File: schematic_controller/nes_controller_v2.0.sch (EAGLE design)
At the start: 22 parts

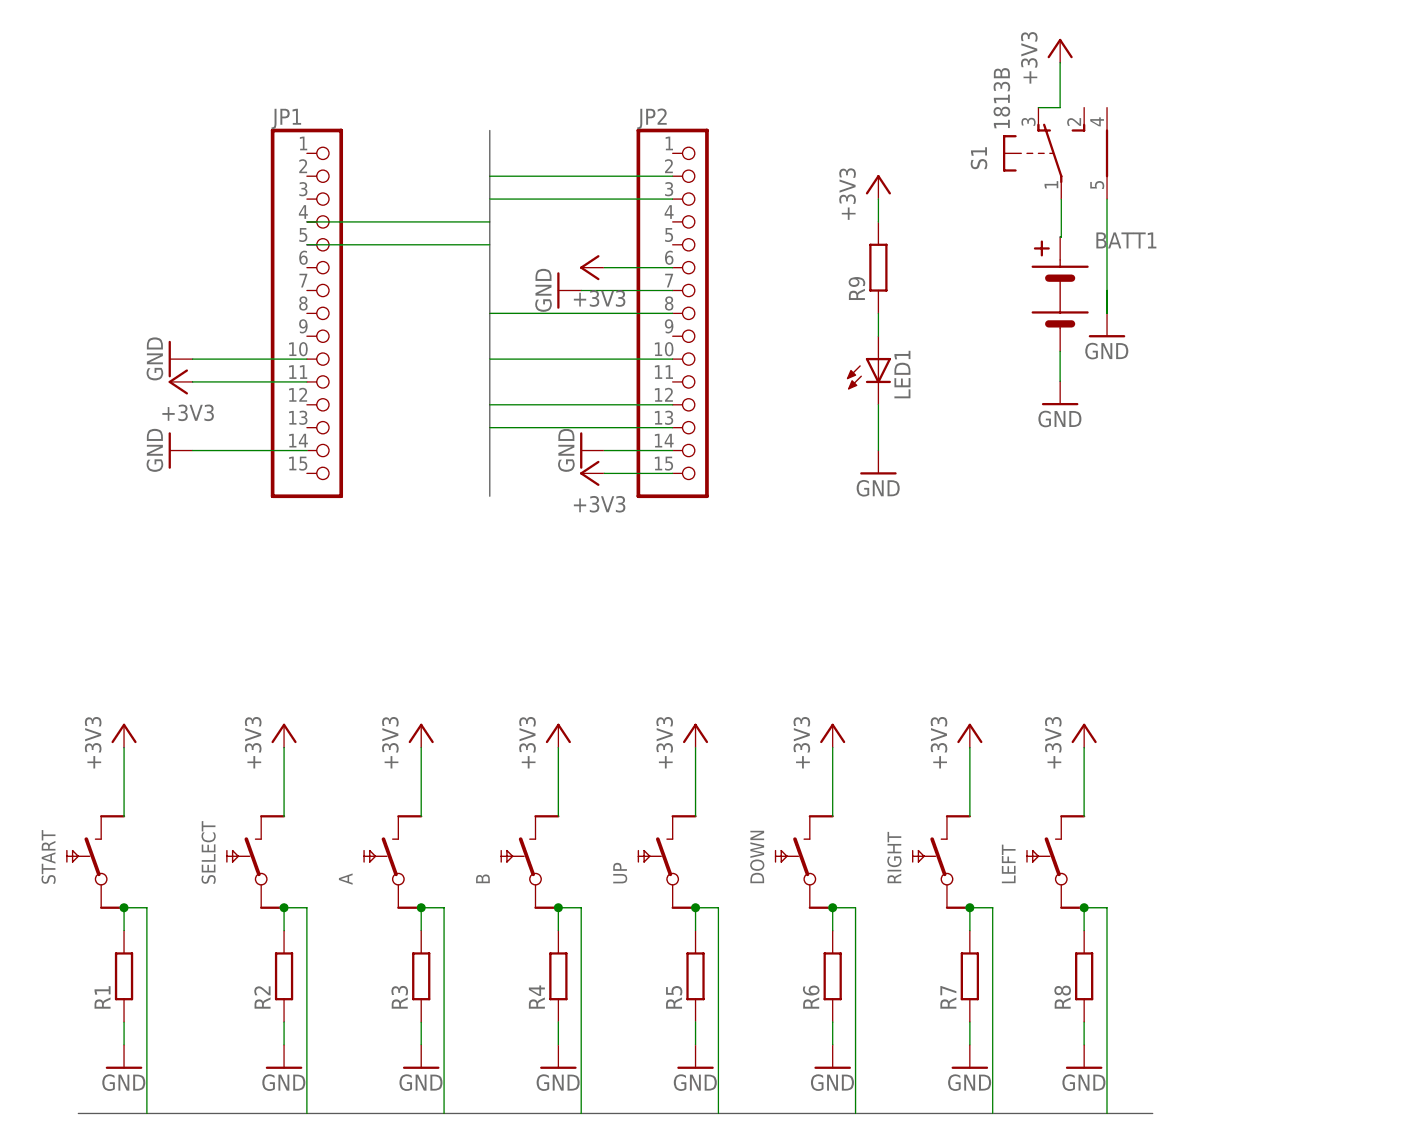
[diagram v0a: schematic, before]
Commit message: changed schematic and boart to v2
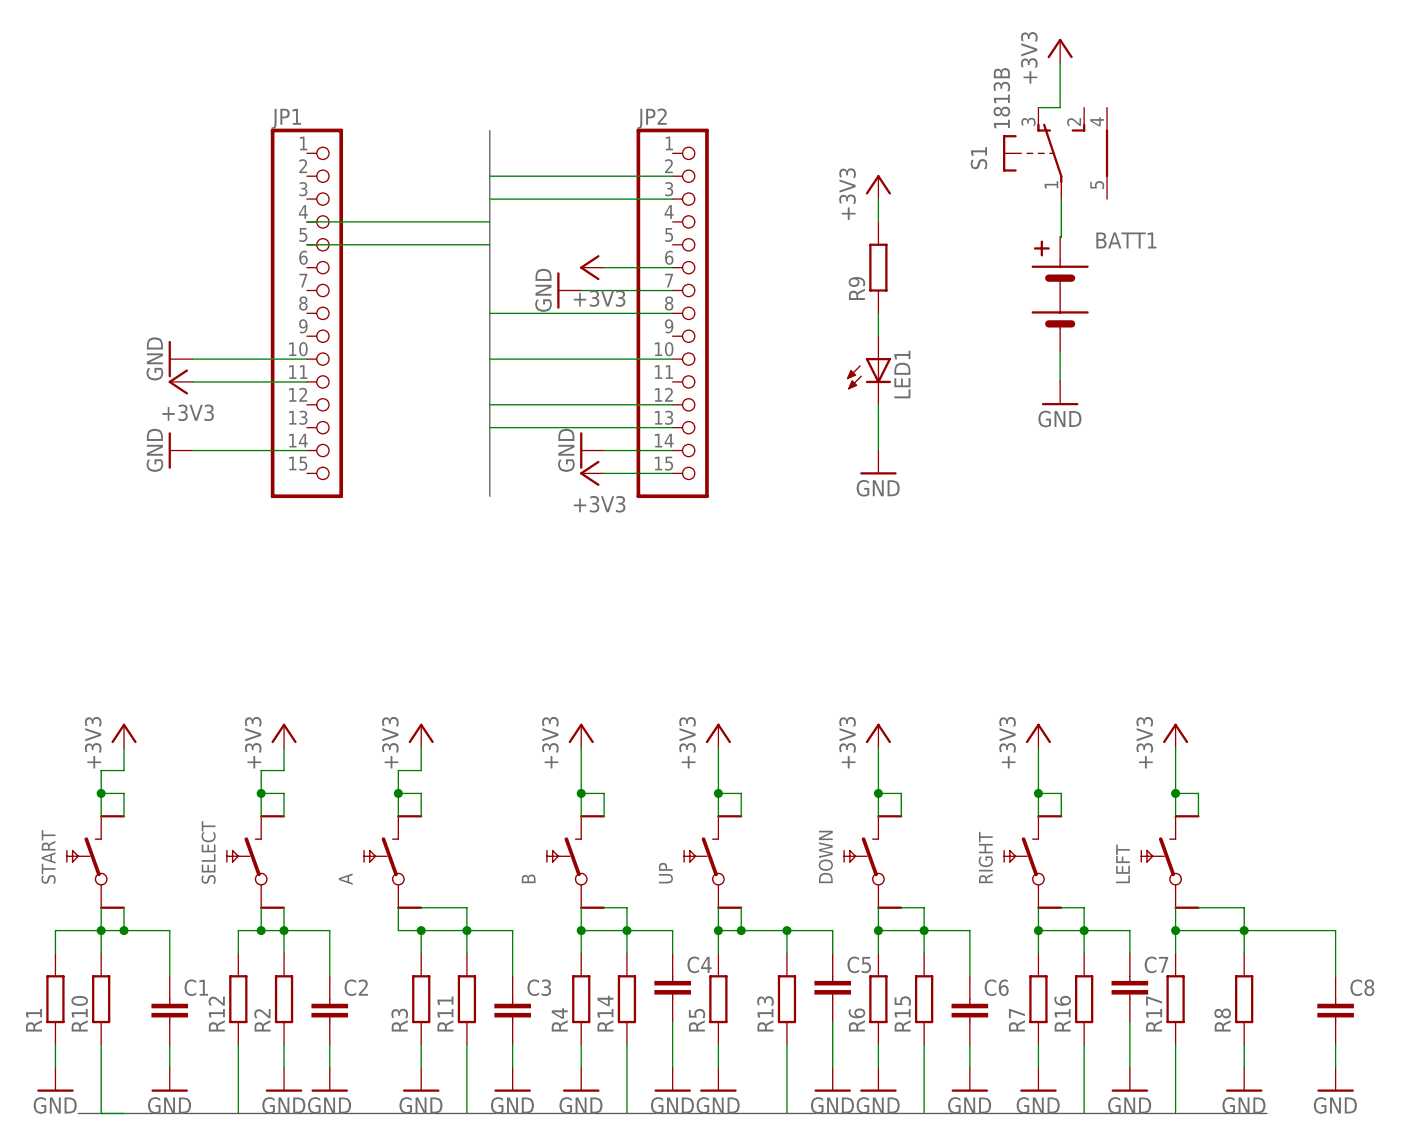
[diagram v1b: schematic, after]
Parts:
- added C1, C2, C3, C4, C5, C6, C7, C8: (no value), rcl:C-EUC0805K
- added R10, R11, R12, R13, R14, R15, R16, R17: (no value), rcl:R-EU_R1206
- R1, R2, R3, R4, R5, R6, R7, R8, R9: device rcl:R-EU_MELF0207R -> rcl:R-EU_R1206
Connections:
- new net 3§4: C2.1, R12.2, R2.2, SELECT.1, SELECT.11
- new net 4$5: A.1, A.11, C3.1, R11.2, R3.2
- new net N$3: C1.1, R1.2, R10.2, START.1, START.11
- new net N$4: B.1, B.11, C4.1, R14.2, R4.2
- new net N$5: C5.1, R13.2, R5.2, UP.1, UP.11
- new net N$6: C6.1, DOWN.1, DOWN.11, R15.2, R6.2
- new net N$7: C7.1, R16.2, R7.2, RIGHT.1, RIGHT.11
- new net N$8: C8.1, LEFT.1, LEFT.11, R17.2, R8.2
- net +3V3: now also A.2, B.2, DOWN.2, LEFT.2, RIGHT.2, SELECT.2, START.2, UP.2
- net A: now also R11.1; no longer A.11, R3.2
- net B: now also R14.1; no longer B.11, R4.2
- net DOWN: now also JP2.10, R15.1; no longer DOWN.11, JP2.8, R6.2
- net GND: now also C1.2, C2.2, C3.2, C4.2, C5.2, C6.2, C7.2, C8.2; no longer S1.SH2
- net LEFT: now also JP2.3, R17.1; no longer JP2.10, LEFT.11, R8.2
- net RIGHT: now also JP2.8, R16.1; no longer JP2.13, R7.2, RIGHT.11
- net SELECT: now also JP2.12, R12.1; no longer JP2.2, R2.2, SELECT.11
- net START: now also JP2.13, R10.1; no longer JP2.3, R1.2, START.11
- net UP: now also JP2.2, R13.1; no longer JP2.12, R5.2, UP.11
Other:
- moved on the sheet: B, DOWN, LEFT, R1, R2, R3, R4, R5, R6, R7, R8, RIGHT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
